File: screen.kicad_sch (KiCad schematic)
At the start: 0 parts

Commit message: pcb-master: improve schematics to be much more organized.
Signed-off-by: Amlal EL Mahrouss <amlalelmahrouss@icloud.com>
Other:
- note added: "ScreenBridge"
- note added: "Touchscreen"
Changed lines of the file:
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@@
 		(company "Zeta")
 	)
+	(rectangle
+		(start 13.97 15.24)
+		(end 166.37 193.04)
+		(stroke
+			(width 0)
+			(type default)
+		)
+		(fill
+			(type none)
+		)
+	)
+	(rectangle
+		(start 170.18 22.86)
+		(end 275.59 154.94)
+		(stroke
+			(width 0)
+			(type default)
+		)
+		(fill
+			(type none)
+		)
+	)
+	(text "ScreenBridge\n"
+		(exclude_from_sim no)
+		(at 180.594 30.226 0)
+		(effects
+			(font
+				(size 1.27 1.27)
+			)
+		)
+	)
+	(text "Touchscreen"
+		(exclude_from_sim no)
+		(at 21.336 22.098 0)
+		(effects
+			(font
+				(size 1.27 1.27)
+			)
+		)
+	)
 )

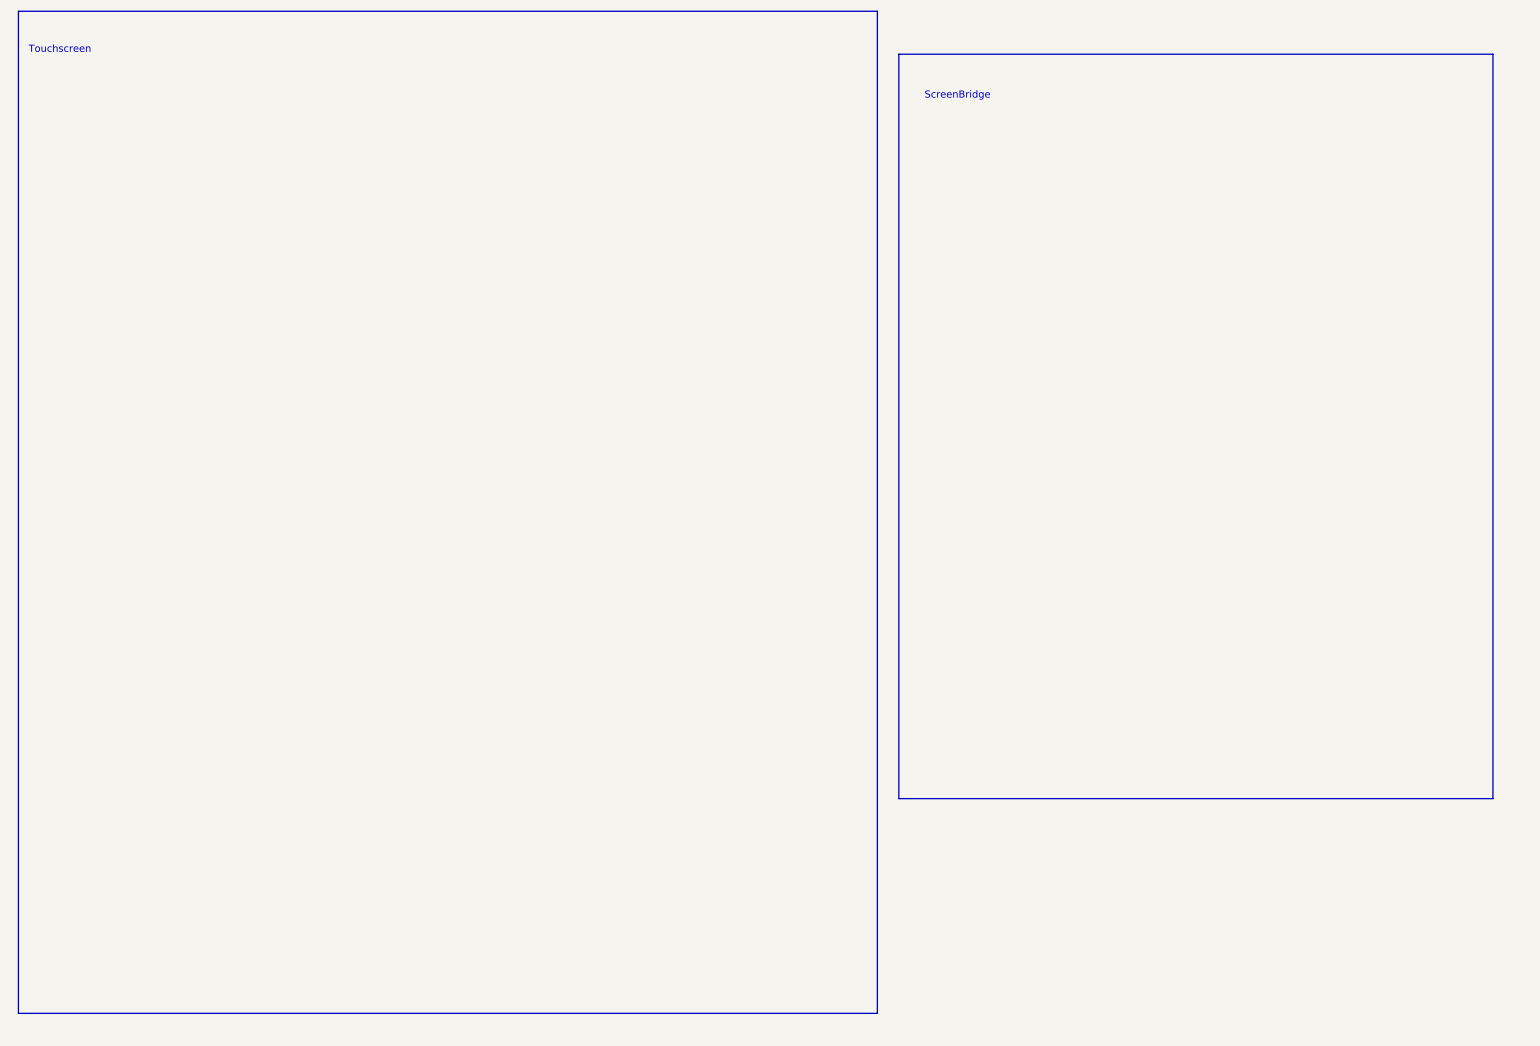
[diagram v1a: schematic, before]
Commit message: pcb-master: improve schematic and PCB.
Signed-off-by: Amlal EL Mahrouss <amlalelmahrouss@icloud.com>
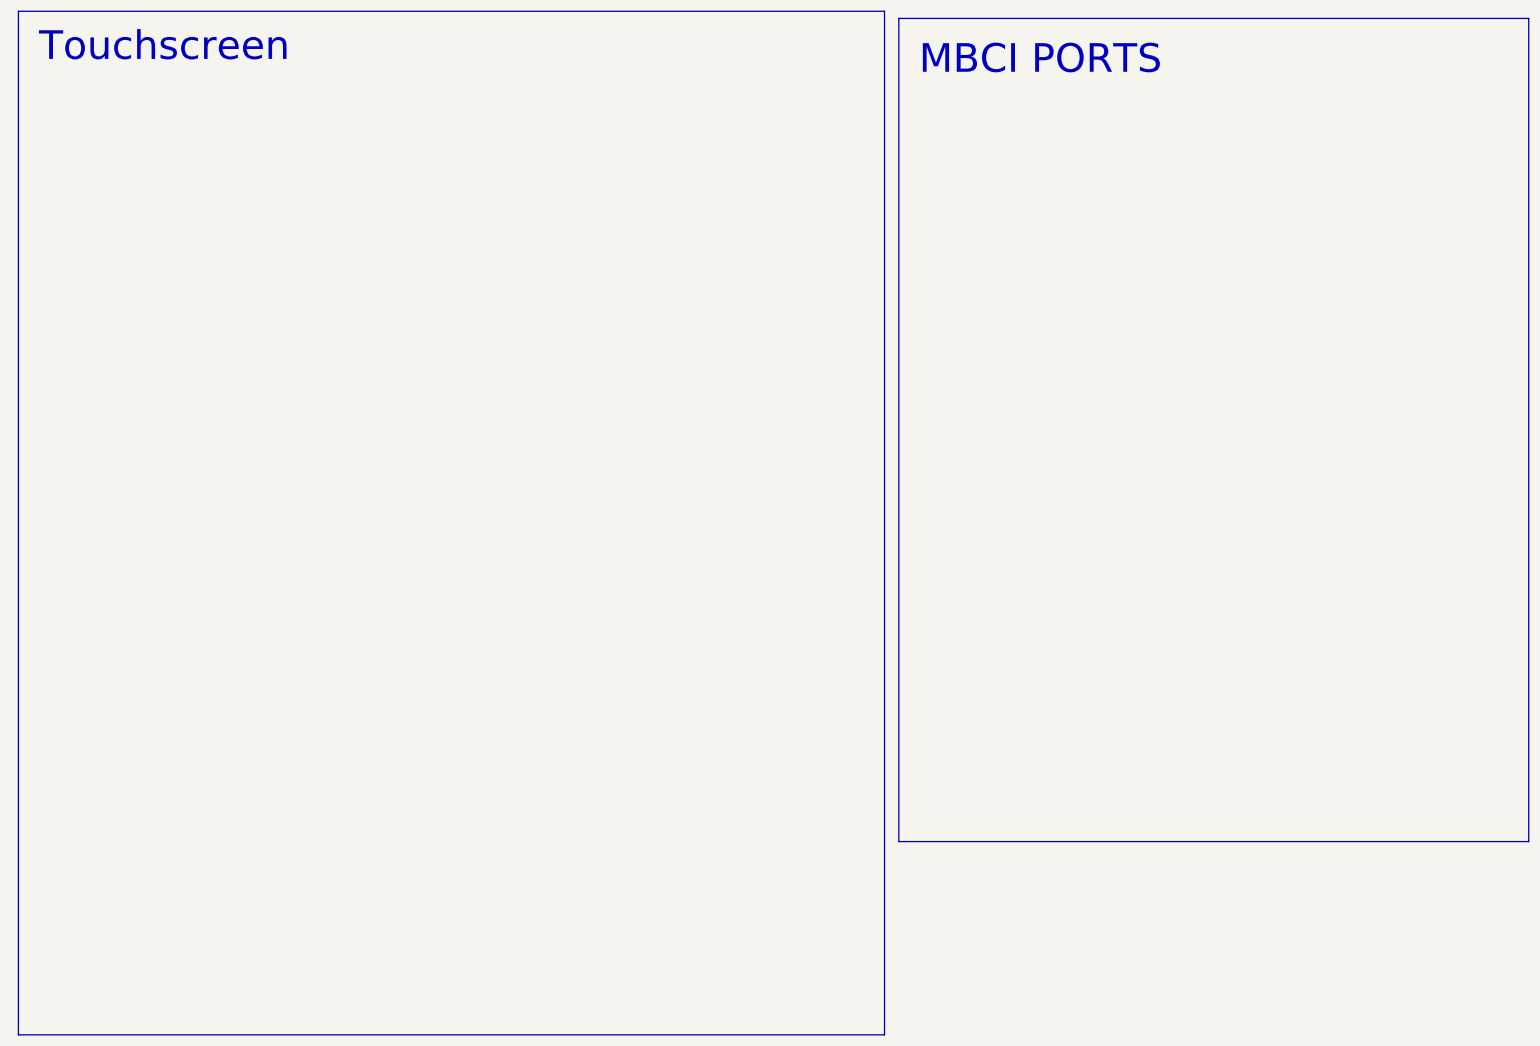
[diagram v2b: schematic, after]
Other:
- note added: "MBCI PORTS"
- note removed: "ScreenBridge"
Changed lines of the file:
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@@
 	(rectangle
 		(start 13.97 15.24)
-		(end 166.37 193.04)
+		(end 167.64 196.85)
 		(stroke
 			(width 0)
@@
 	)
 	(rectangle
-		(start 170.18 22.86)
-		(end 275.59 154.94)
+		(start 170.18 16.51)
+		(end 281.94 162.56)
 		(stroke
 			(width 0)
@@
 		)
 	)
-	(text "ScreenBridge\n"
+	(text "Touchscreen"
 		(exclude_from_sim no)
-		(at 180.594 30.226 0)
+		(at 39.878 21.59 0)
 		(effects
 			(font
-				(size 1.27 1.27)
+				(size 5.08 5.08)
 			)
 		)
 	)
-	(text "Touchscreen"
+	(text "MBCI PORTS"
 		(exclude_from_sim no)
-		(at 21.336 22.098 0)
+		(at 195.326 23.876 0)
 		(effects
 			(font
-				(size 1.27 1.27)
+				(size 5.08 5.08)
 			)
 		)

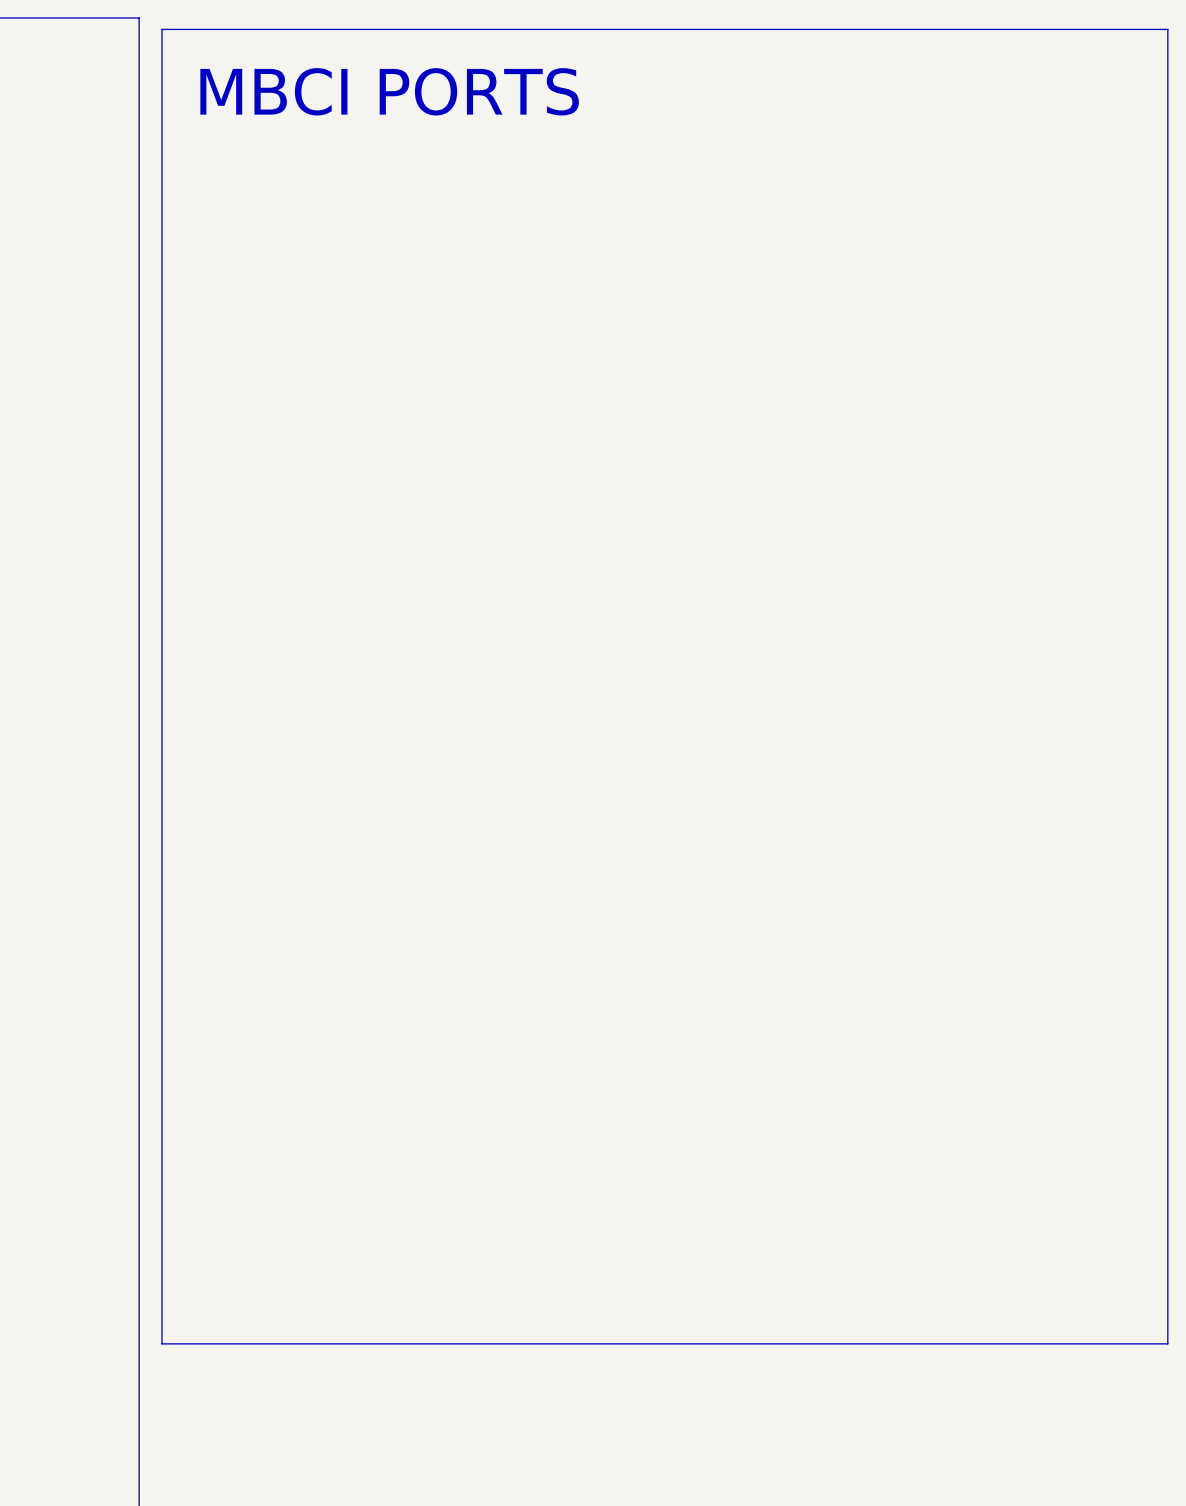
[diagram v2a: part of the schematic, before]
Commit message: FIX: Schematic and PCB, Improved those and regenerated zones as well.
Signed-off-by: Amlal EL Mahrouss <amlalelmahrouss@icloud.com>
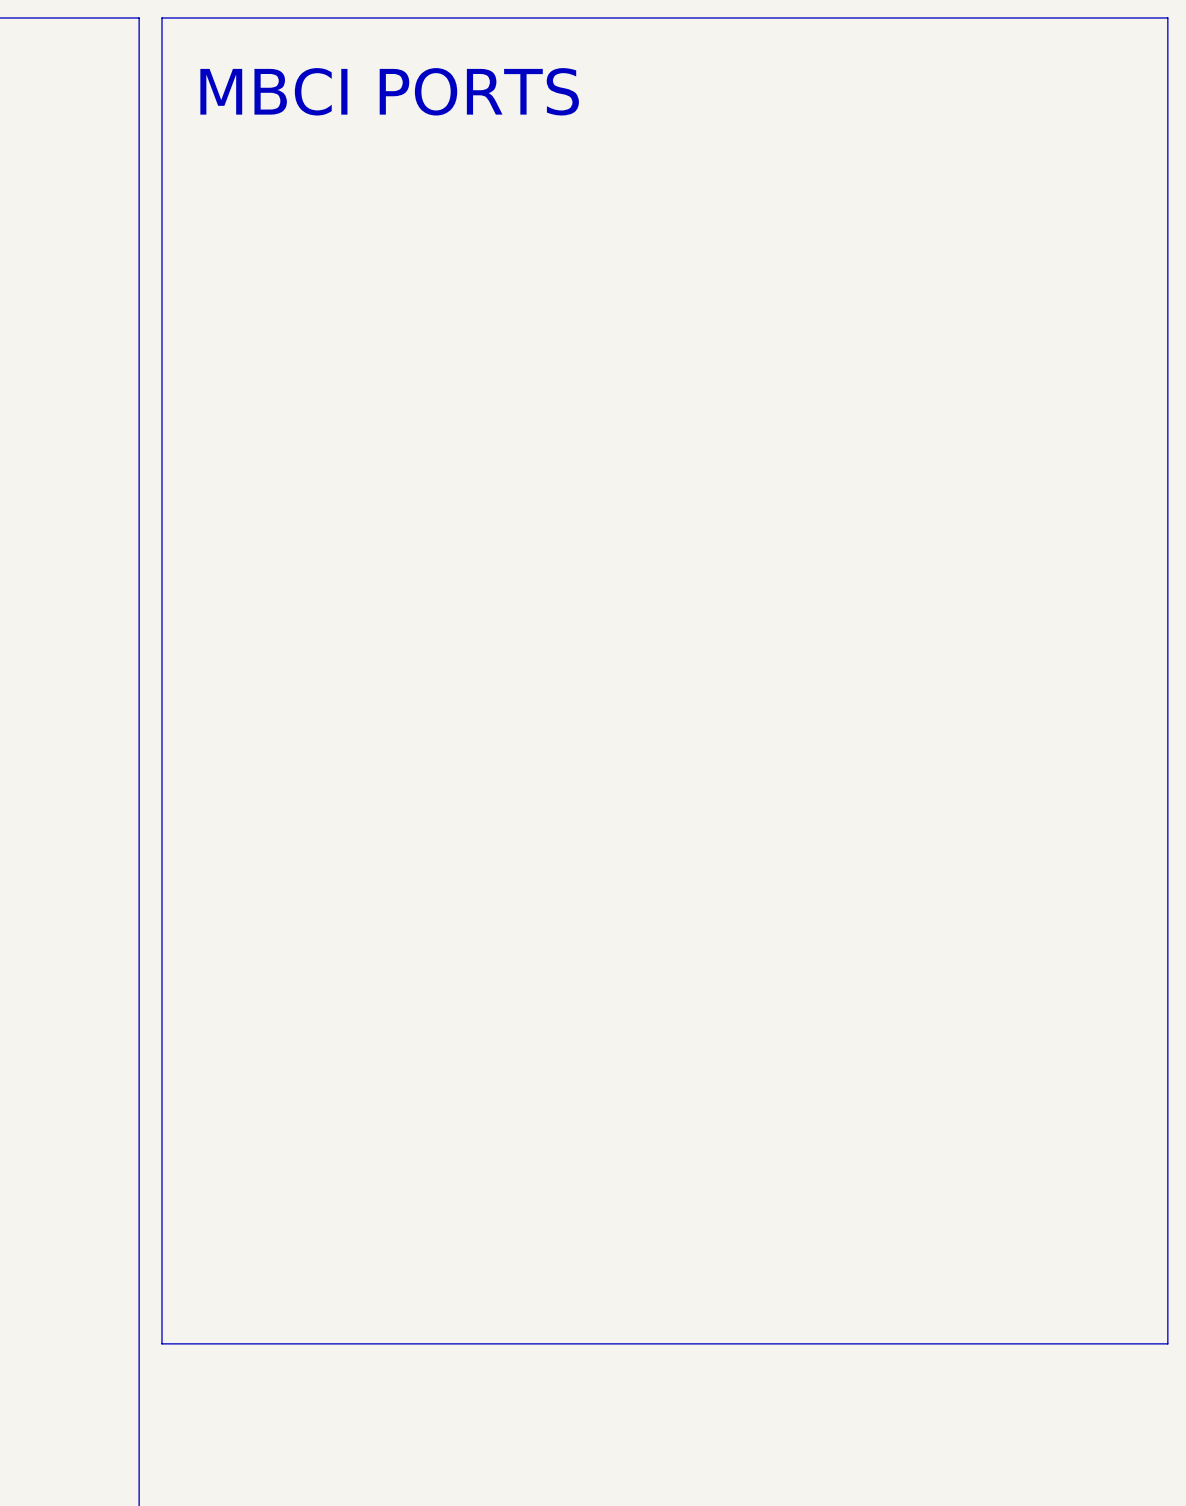
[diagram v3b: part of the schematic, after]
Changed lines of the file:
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@@
 	)
 	(rectangle
-		(start 170.18 16.51)
+		(start 170.18 15.24)
 		(end 281.94 162.56)
 		(stroke
